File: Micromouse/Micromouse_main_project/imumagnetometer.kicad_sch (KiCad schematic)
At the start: 9 parts, among them U4 ICM-42688-P, U5 LIS2MDLTR

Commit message: Prepped layout
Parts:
- removed C26: 220n, Capacitor_SMD:C_0603_1608Metric, symbol Device:C
- removed C27, C28: 100n, Capacitor_SMD:C_0603_1608Metric, symbol Device:C
- removed C29: 10u, Capacitor_SMD:C_0603_1608Metric, symbol Device:C
- removed U5: LIS2MDLTR, MM_LIS2MDLTR:LIS2MDLTR, symbol LIS2MDLTR:LIS2MDLTR
- added J15: Conn_01x07_Pin, Connector_PinSocket_2.54mm:PinSocket_1x07_P2.54mm_Vertical, symbol Connector:Conn_01x07_Pin
- U4: footprint MM_ICM_42688_P:ICM_42688_P -> ICM_42688_P_FOOTPRINT:ICM_42688_P
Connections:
- net 3.3V: now also J15.7 (Pin_7)
- net GND: now also J15.5 (Pin_5)
- net INT_MAG: now also J15.2 (Pin_2)
- net MAG_SCL: now also J15.4 (Pin_4)
- net MAG_SDA: now also J15.3 (Pin_3)
- no-connect marks 6 -> 5
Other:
- note added: "CS pulled up internally"
- note added: "LIS2MDL breakout board"
- note added: "internal 3.3V LDO (not needed)"
- note removed: "Magnetometer"

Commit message: Finished layout
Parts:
- renumbered C23 to C21, C24 to C22, C25 to C23, J15 to J9
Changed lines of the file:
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@@
 		(in_pos_files yes)
 		(dnp no)
-		(property "Reference" "C23"
+		(property "Reference" "C21"
 			(at 141.224 85.09 0)
 			(show_name no)
@@
 			(project "MicromouseSchematic"
 				(path "/0dcfab91-6b00-43c0-ac0b-8c301cb559e5/020b5f85-8a9d-45f7-80e4-737602419b71"
-					(reference "C23")
+					(reference "C21")
 					(unit 1)
 				)
@@
 		(dnp no)
 		(fields_autoplaced yes)
-		(property "Reference" "#PWR035"
+		(property "Reference" "#PWR036"
 			(at 134.62 104.14 0)
 			(hide yes)
@@
 			(project "MicromouseSchematic"
 				(path "/0dcfab91-6b00-43c0-ac0b-8c301cb559e5/020b5f85-8a9d-45f7-80e4-737602419b71"
-					(reference "#PWR035")
+					(reference "#PWR036")
 					(unit 1)
 				)
@@
 		(dnp no)
 		(fields_autoplaced yes)
-		(property "Reference" "J15"
+		(property "Reference" "J9"
 			(at 209.55 76.1999 0)
 			(show_name no)
@@
 			(project "MicromouseSchematic"
 				(path "/0dcfab91-6b00-43c0-ac0b-8c301cb559e5/020b5f85-8a9d-45f7-80e4-737602419b71"
-					(reference "J15")
+					(reference "J9")
 					(unit 1)
 				)
@@
 		(in_pos_files yes)
 		(dnp no)
-		(property "Reference" "C24"
+		(property "Reference" "C22"
 			(at 151.13 85.09 0)
 			(show_name no)
@@
 			(project "MicromouseSchematic"
 				(path "/0dcfab91-6b00-43c0-ac0b-8c301cb559e5/020b5f85-8a9d-45f7-80e4-737602419b71"
-					(reference "C24")
+					(reference "C22")
 					(unit 1)
 				)
@@
 		(in_pos_files yes)
 		(dnp no)
-		(property "Reference" "C25"
+		(property "Reference" "C23"
 			(at 162.052 85.09 0)
 			(show_name no)
@@
 			(project "MicromouseSchematic"
 				(path "/0dcfab91-6b00-43c0-ac0b-8c301cb559e5/020b5f85-8a9d-45f7-80e4-737602419b71"
-					(reference "C25")
+					(reference "C23")
 					(unit 1)
 				)
@@
 		(dnp no)
 		(fields_autoplaced yes)
-		(property "Reference" "#PWR036"
+		(property "Reference" "#PWR037"
 			(at 193.04 74.93 0)
 			(hide yes)
@@
 			(project "MicromouseSchematic"
 				(path "/0dcfab91-6b00-43c0-ac0b-8c301cb559e5/020b5f85-8a9d-45f7-80e4-737602419b71"
-					(reference "#PWR036")
+					(reference "#PWR037")
 					(unit 1)
 				)

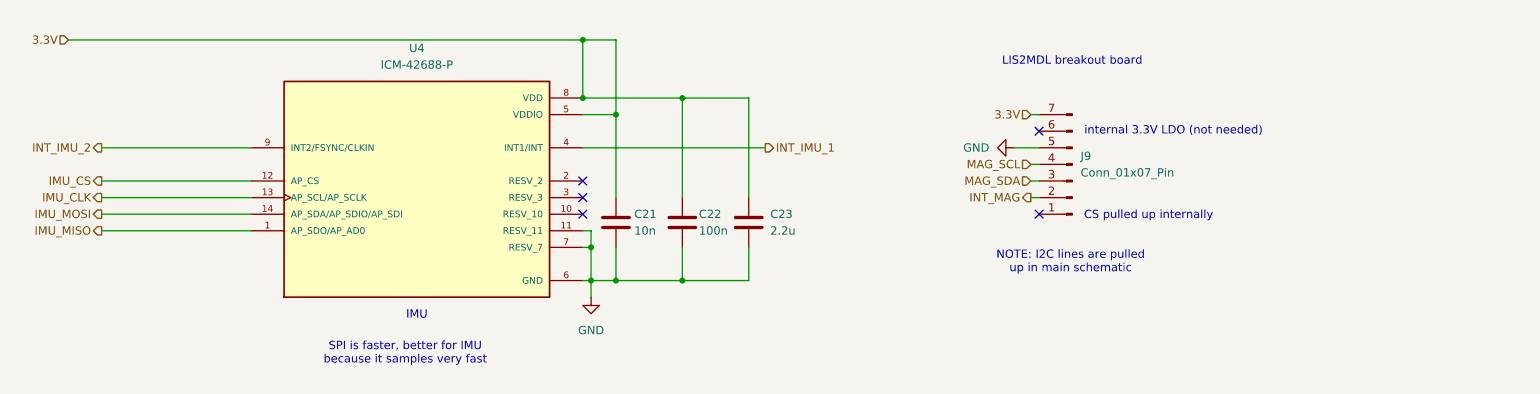
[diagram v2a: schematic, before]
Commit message: Completed IR board, ToF board, changed IMU
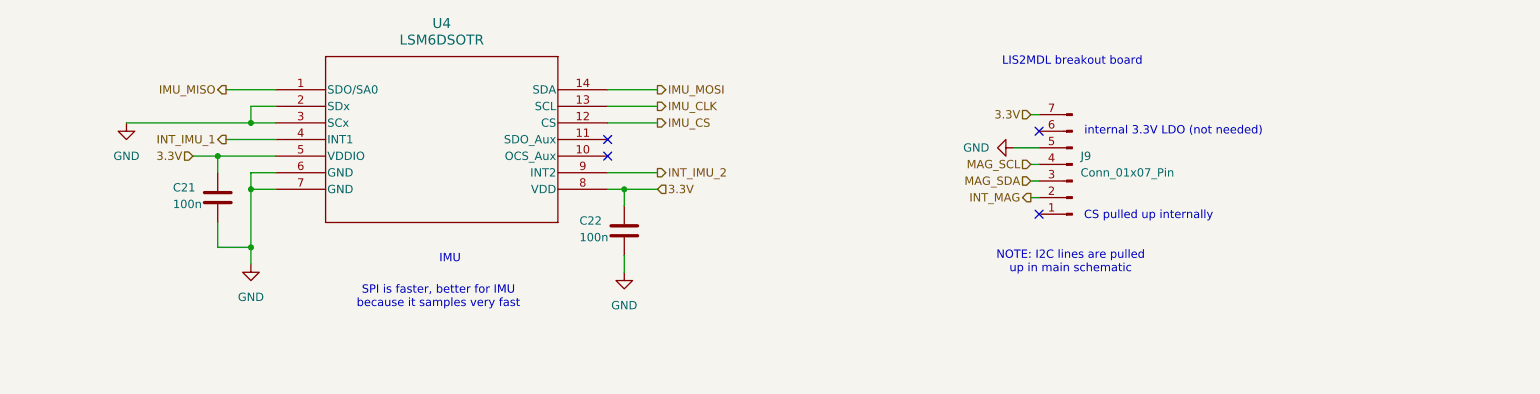
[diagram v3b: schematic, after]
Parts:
- removed C23: 2.2u, Capacitor_SMD:C_0603_1608Metric, symbol Device:C
- removed U4: ICM-42688-P, ICM_42688_P_FOOTPRINT:ICM_42688_P, symbol ICM-42688-P:ICM-42688-P
- added U4: LSM6DSOTR, MM_LSM6DSOTR:LGA-14L_2P5X3X0P86_STM, symbol LSM6DSOTR:LSM6DSOTR
- C21: value 10n -> 100n
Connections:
- net 3.3V: now also U4.5 (VDDIO), U4.8 (VDD)
- net GND: now also U4.2 (SDx), U4.3 (SCx), U4.6 (GND), U4.7 (GND)
- net IMU_CLK: now also U4.13 (SCL)
- net IMU_CS: now also U4.12 (CS)
- net IMU_MISO: now also U4.1 (SDO/SA0)
- net IMU_MOSI: now also U4.14 (SDA)
- net INT_IMU_1: now also U4.4 (INT1)
- net INT_IMU_2: now also U4.9 (INT2)
- no-connect marks 5 -> 4
